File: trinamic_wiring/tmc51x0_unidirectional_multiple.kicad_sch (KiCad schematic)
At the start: 2 parts

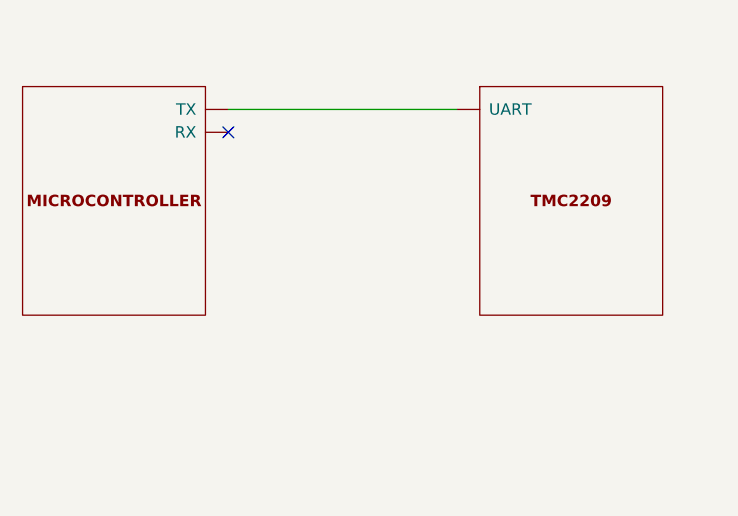
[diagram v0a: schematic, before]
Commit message: Add TMC51X0 files
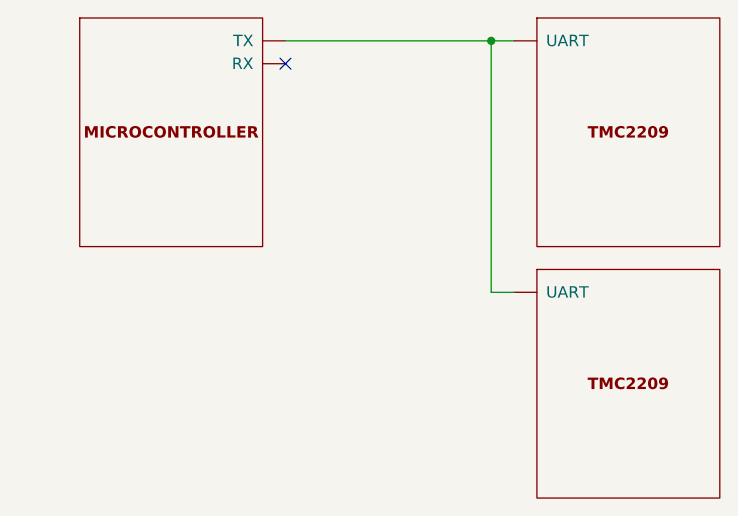
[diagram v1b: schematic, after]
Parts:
- removed MICROCONTROLLER4: DOC_MCU, symbol Janelia:DOC_MCU
- removed TMC6: DOC_TMC2209, symbol Janelia:DOC_TMC2209
- added MICROCONTROLLER1: DOC_MCU, symbol Janelia:DOC_MCU
- added TMC1, TMC8: DOC_TMC2209, symbol Janelia:DOC_TMC2209
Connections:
- new net: MICROCONTROLLER1.1 (TX), TMC1.0 (UART), TMC8.0 (UART)
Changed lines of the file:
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@@
     (company "Janelia Research Campus")
   )
-  (no_connect (at 119.38 87.63))
-  (wire (pts (xy 119.38 85.09) (xy 144.78 85.09))
+  (junction (at 148.59 77.47) (diameter 0) (color 0 0 0 0)
+  )
+  (no_connect (at 125.73 80.01))
+  (wire (pts (xy 148.59 77.47) (xy 151.13 77.47))
     (stroke (width 0) (type default))
   )
-  (symbol (lib_id "Janelia:DOC_MCU") (at 106.68 95.25 0) (unit 1)
+  (wire (pts (xy 148.59 77.47) (xy 148.59 105.41))
+    (stroke (width 0) (type default))
+  )
+  (wire (pts (xy 125.73 77.47) (xy 148.59 77.47))
+    (stroke (width 0) (type default))
+  )
+  (wire (pts (xy 148.59 105.41) (xy 151.13 105.41))
+    (stroke (width 0) (type default))
+  )
+  (symbol (lib_id "Janelia:DOC_TMC2209") (at 163.83 115.57 0) (unit 1)
     (in_bom yes) (on_board yes) (dnp no) (fields_autoplaced)
-    (property "Reference" "MICROCONTROLLER4" (at 106.68 76.2 0)
+    (property "Reference" "TMC8" (at 163.83 96.52 0)
       (effects (font (size 1.27 1.27)) hide)
     )
-    (property "Value" "DOC_MCU" (at 106.68 81.28 0)
+    (property "Value" "DOC_TMC2209" (at 163.83 101.6 0)
       (effects (font (size 1.524 1.524)) hide)
     )
-    (property "Footprint" "" (at 104.14 121.92 0)
+    (property "Footprint" "" (at 161.29 142.24 0)
       (effects (font (size 1.524 1.524)) hide)
     )
-    (property "Datasheet" "" (at 106.68 95.25 0)
+    (property "Datasheet" "" (at 163.83 115.57 0)
       (effects (font (size 1.524 1.524)) hide)
     )
-    (property "Sim.Enable" "0" (at 106.68 78.74 0)
-      (effects (font (size 1.27 1.27)) hide)
-    )
-    (pin "0")
-    (pin "1")
-    (pin "2")
-    (pin "3")
-    (pin "4")
-    (pin "5")
-    (pin "6")
-    (pin "7")
-    (pin "8")
-    (instances
-      (project "trinamic_wiring"
-        (path "/e4144788-6304-493f-818e-5d881d3b7418/c8eda2b5-ab13-4033-82d9-875c9fcaf884/13e2a7b5-46df-44bb-8dde-5d79d190b8bf"
-          (reference "MICROCONTROLLER4") (unit 1)
-        )
-        (path "/e4144788-6304-493f-818e-5d881d3b7418/a161638e-a96f-4455-865a-1d7502675f43/13e2a7b5-46df-44bb-8dde-5d79d190b8bf"
-          (reference "MICROCONTROLLER4") (unit 1)
-        )
-      )
-    )
-  )
-  (symbol (lib_id "Janelia:DOC_TMC2209") (at 157.48 95.25 0) (unit 1)
-    (in_bom yes) (on_board yes) (dnp no) (fields_autoplaced)
-    (property "Reference" "TMC6" (at 157.48 76.2 0)
-      (effects (font (size 1.27 1.27)) hide)
-    )
-    (property "Value" "DOC_TMC2209" (at 157.48 81.28 0)
-      (effects (font (size 1.524 1.524)) hide)
-    )
-    (property "Footprint" "" (at 154.94 121.92 0)
-      (effects (font (size 1.524 1.524)) hide)
-    )
-    (property "Datasheet" "" (at 157.48 95.25 0)
-      (effects (font (size 1.524 1.524)) hide)
-    )
-    (property "Sim.Enable" "0" (at 157.48 78.74 0)
+    (property "Sim.Enable" "0" (at 163.83 99.06 0)
       (effects (font (size 1.27 1.27)) hide)
     )
@@
     (instances
       (project "trinamic_wiring"
-        (path "/e4144788-6304-493f-818e-5d881d3b7418/c8eda2b5-ab13-4033-82d9-875c9fcaf884/13e2a7b5-46df-44bb-8dde-5d79d190b8bf"
-          (reference "TMC6") (unit 1)
+        (path "/e4144788-6304-493f-818e-5d881d3b7418/c8eda2b5-ab13-4033-82d9-875c9fcaf884/5b0a2695-6b0b-4c82-b9d6-7e19fee75501"
+          (reference "TMC8") (unit 1)
         )
-        (path "/e4144788-6304-493f-818e-5d881d3b7418/a161638e-a96f-4455-865a-1d7502675f43/13e2a7b5-46df-44bb-8dde-5d79d190b8bf"
-          (reference "TMC6") (unit 1)
+        (path "/e4144788-6304-493f-818e-5d881d3b7418/a161638e-a96f-4455-865a-1d7502675f43/5b0a2695-6b0b-4c82-b9d6-7e19fee75501"
+          (reference "TMC8") (unit 1)
         )
       )
+    )
+  )
+  (symbol (lib_id "Janelia:DOC_TMC2209") (at 163.83 87.63 0) (unit 1)
+    (in_bom yes) (on_board yes) (dnp no) (fields_autoplaced)
+    (property "Reference" "TMC1" (at 163.83 68.58 0)
+      (effects (font (size 1.27 1.27)) hide)
+    )
+    (property "Value" "DOC_TMC2209" (at 163.83 73.66 0)
+      (effects (font (size 1.524 1.524)) hide)
+    )
+    (property "Footprint" "" (at 161.29 114.3 0)
+      (effects (font (size 1.524 1.524)) hide)
+    )
+    (property "Datasheet" "" (at 163.83 87.63 0)
+      (effects (font (size 1.524 1.524)) hide)
+    )
+    (property "Sim.Enable" "0" (at 163.83 71.12 0)
+      (effects (font (size 1.27 1.27)) hide)
+    )
+    (pin "0")
+    (pin "1")
+    (pin "10")
+    (pin "2")
+    (pin "3")
+    (pin "4")
+    (pin "5")
+    (pin "6")
+    (pin "7")
+    (pin "8")
+    (pin "9")
+    (instances
+      (project "trinamic_wiring"
+        (path "/e4144788-6304-493f-818e-5d881d3b7418/c8eda2b5-ab13-4033-82d9-875c9fcaf884/5b0a2695-6b0b-4c82-b9d6-7e19fee75501"
+          (reference "TMC1") (unit 1)
+        )
+        (path "/e4144788-6304-493f-818e-5d881d3b7418/a161638e-a96f-4455-865a-1d7502675f43/5b0a2695-6b0b-4c82-b9d6-7e19fee75501"
+          (reference "TMC1") (unit 1)
+        )
+      )
+    )
+  )
+  (symbol (lib_id "Janelia:DOC_MCU") (at 113.03 87.63 0) (unit 1)
+    (in_bom yes) (on_board yes) (dnp no) (fields_autoplaced)
+    (property "Reference" "MICROCONTROLLER1" (at 113.03 68.58 0)
+      (effects (font (size 1.27 1.27)) hide)
+    )
+    (property "Value" "DOC_MCU" (at 113.03 73.66 0)
+      (effects (font (size 1.524 1.524)) hide)
+    )
+    (property "Footprint" "" (at 110.49 114.3 0)
+      (effects (font (size 1.524 1.524)) hide)
+    )
+    (property "Datasheet" "" (at 113.03 87.63 0)
+      (effects (font (size 1.524 1.524)) hide)
+    )
+    (property "Sim.Enable" "0" (at 113.03 71.12 0)
+      (effects (font (size 1.27 1.27)) hide)
+    )
+    (pin "0")
+    (pin "1")
+    (pin "2")
+    (pin "3")
+    (pin "4")
+    (pin "5")
+    (pin "6")
+    (pin "7")
+    (pin "8")
+    (instances
+      (project "trinamic_wiring"
+        (path "/e4144788-6304-493f-818e-5d881d3b7418/c8eda2b5-ab13-4033-82d9-875c9fcaf884/5b0a2695-6b0b-4c82-b9d6-7e19fee75501"
+          (reference "MICROCONTROLLER1") (unit 1)
+        )
+        (path "/e4144788-6304-493f-818e-5d881d3b7418/a161638e-a96f-4455-865a-1d7502675f43/5b0a2695-6b0b-4c82-b9d6-7e19fee75501"
+          (reference "MICROCONTROLLER1") (unit 1)
+        )
+      )
